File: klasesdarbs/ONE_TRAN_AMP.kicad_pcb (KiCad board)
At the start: 2 copper layers, 52.1 x 30.5 mm, 11 parts, among them J1 Signal in, J2 Signal out, J3 Power, Q1 BC547

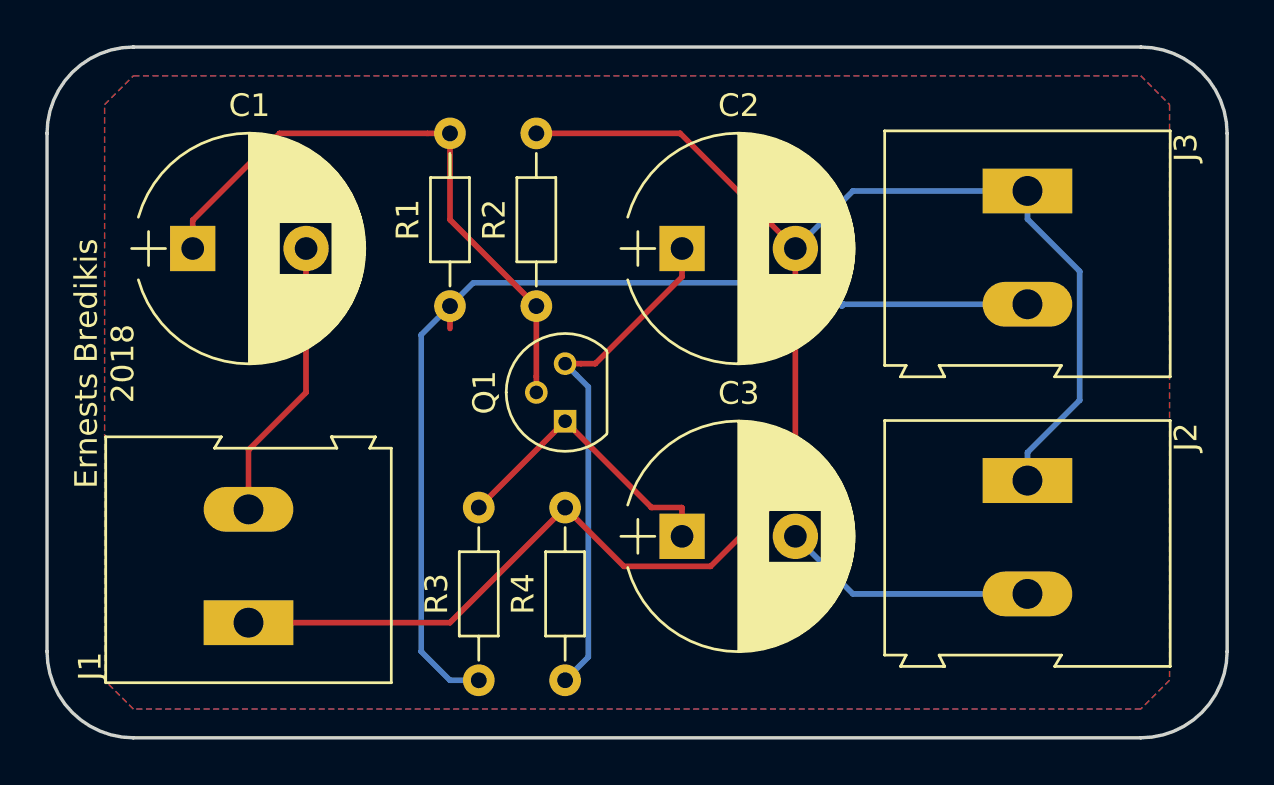
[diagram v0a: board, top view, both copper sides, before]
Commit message: track design corected
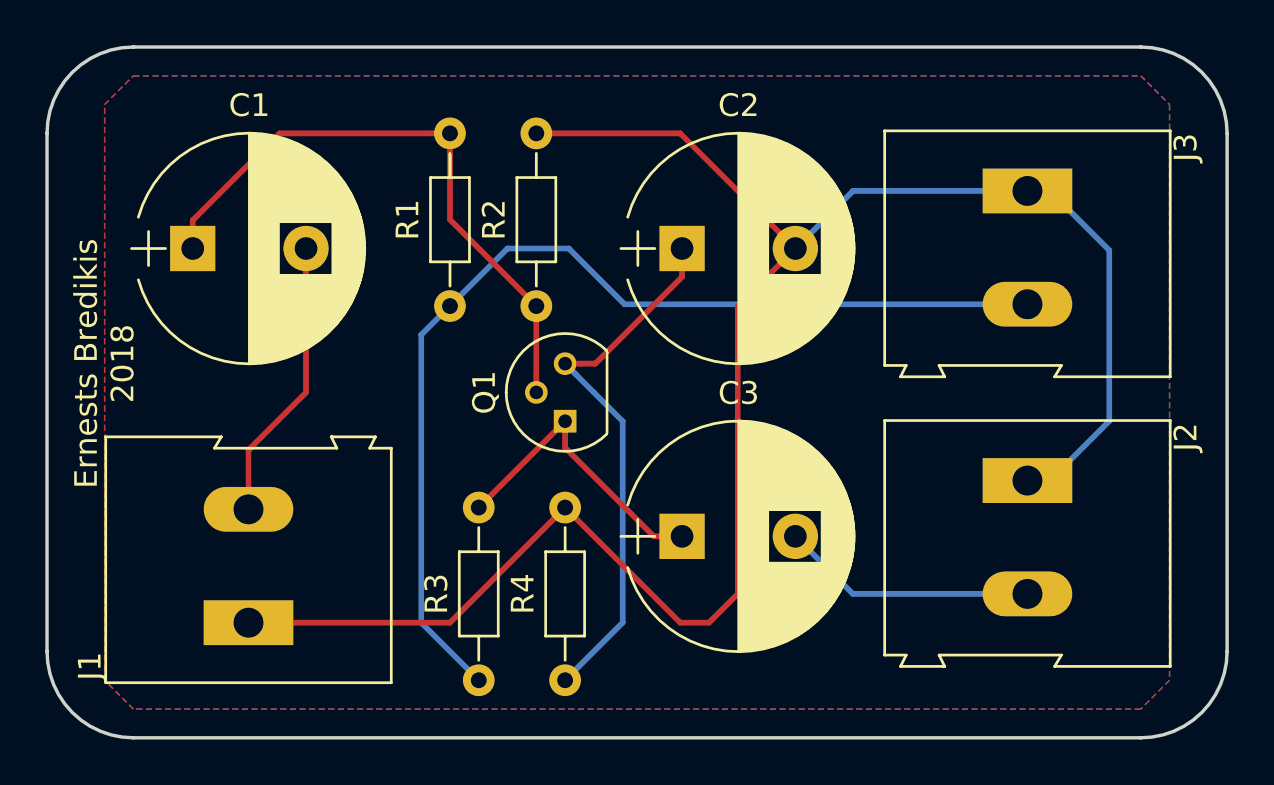
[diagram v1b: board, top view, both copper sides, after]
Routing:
- net GND: track 78.7 -> 84.4 mm
- net Net-(C2-Pad1): track 22.8 -> 24.8 mm
- net Net-(C3-Pad1): track 13.4 -> 14.2 mm
- net Net-(J3-Pad2): track 46.2 -> 45.6 mm

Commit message: With tracks
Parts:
- moved R3 16.3 mm to (148.6, 105.4), turned to 270 degrees
- moved R4 16.3 mm to (152.4, 105.4), turned to 270 degrees
- moved R1 11.4 mm to (148.6, 101.6)
- moved R2 11.4 mm to (152.4, 101.6)
- moved C2 10.2 mm to (137.2, 97.8)
- moved C3 9.06 mm to (138.4, 113.0)
- moved Q1 1.80 mm to (143.5, 105.4), turned to 0 degrees
- moved C1 1.27 mm to (125.8, 97.8)
- moved J2 0.11 mm to (162.6, 109.2)
- moved J3 0.08 mm to (162.6, 96.5)
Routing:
- net GND: track 84.4 -> 0.00 mm
- net Net-(J3-Pad2): track 45.6 -> 18.9 mm
- net Net-(C1-Pad1): track 27.2 -> 45.0 mm
- net Net-(C3-Pad2): track 11.3 -> 20.2 mm
- net Net-(C3-Pad1): track 14.2 -> 16.9 mm
- net Net-(C2-Pad1): track 24.8 -> 22.8 mm
- net Net-(C1-Pad2): track 12.6 -> 13.8 mm
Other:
- net class Power: trace_width 0.5 -> 0.3
